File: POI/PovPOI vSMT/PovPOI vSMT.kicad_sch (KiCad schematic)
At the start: 22 parts, among them J2 Conn_01x08, J3 Conn_01x04, J4 Conn_01x08, J5 Conn_01x04, Q1 Q_NMOS_GDSD, SW1 SW_SPST, SW2 SW_SPST, U2 ADXL345BCCZ-RL7

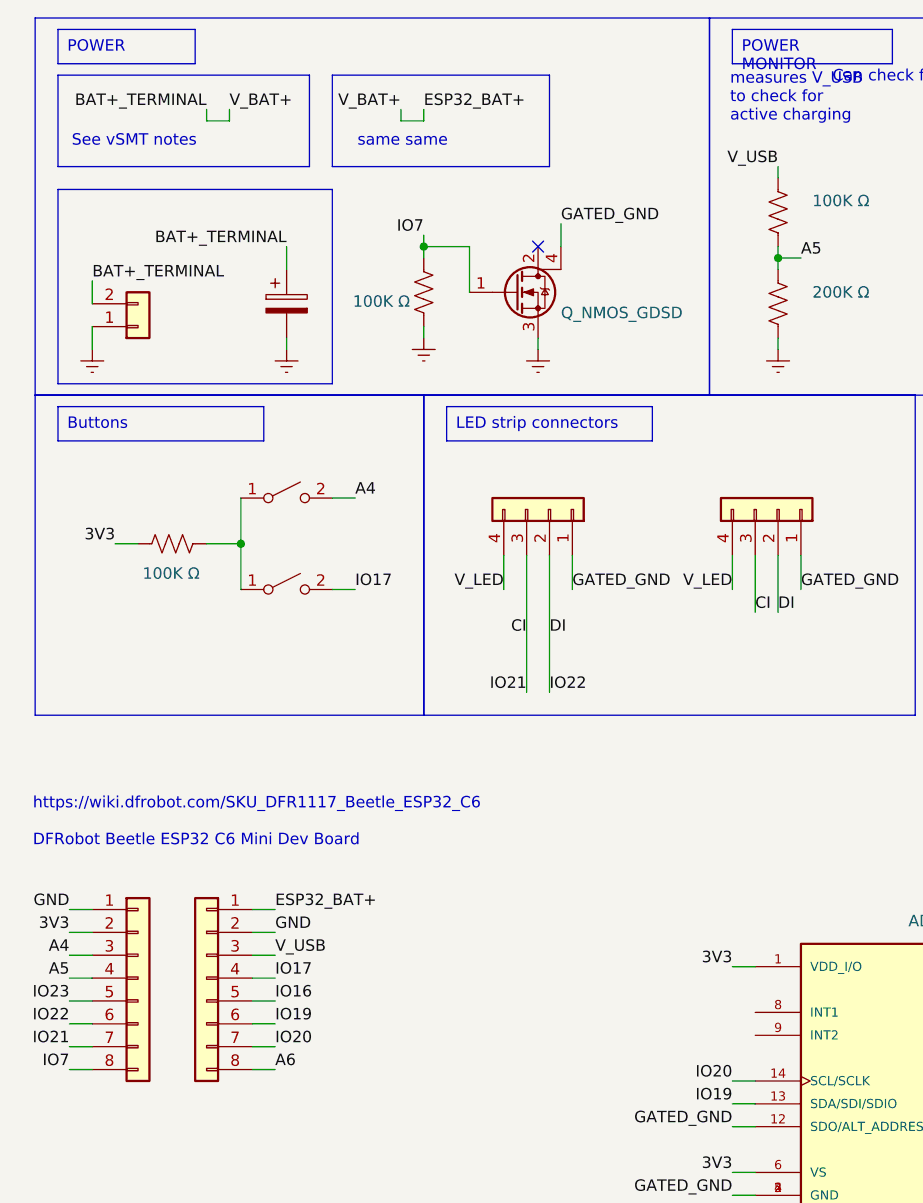
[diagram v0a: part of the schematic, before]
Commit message: Reloaded PovPOI vSMT from worklaptop
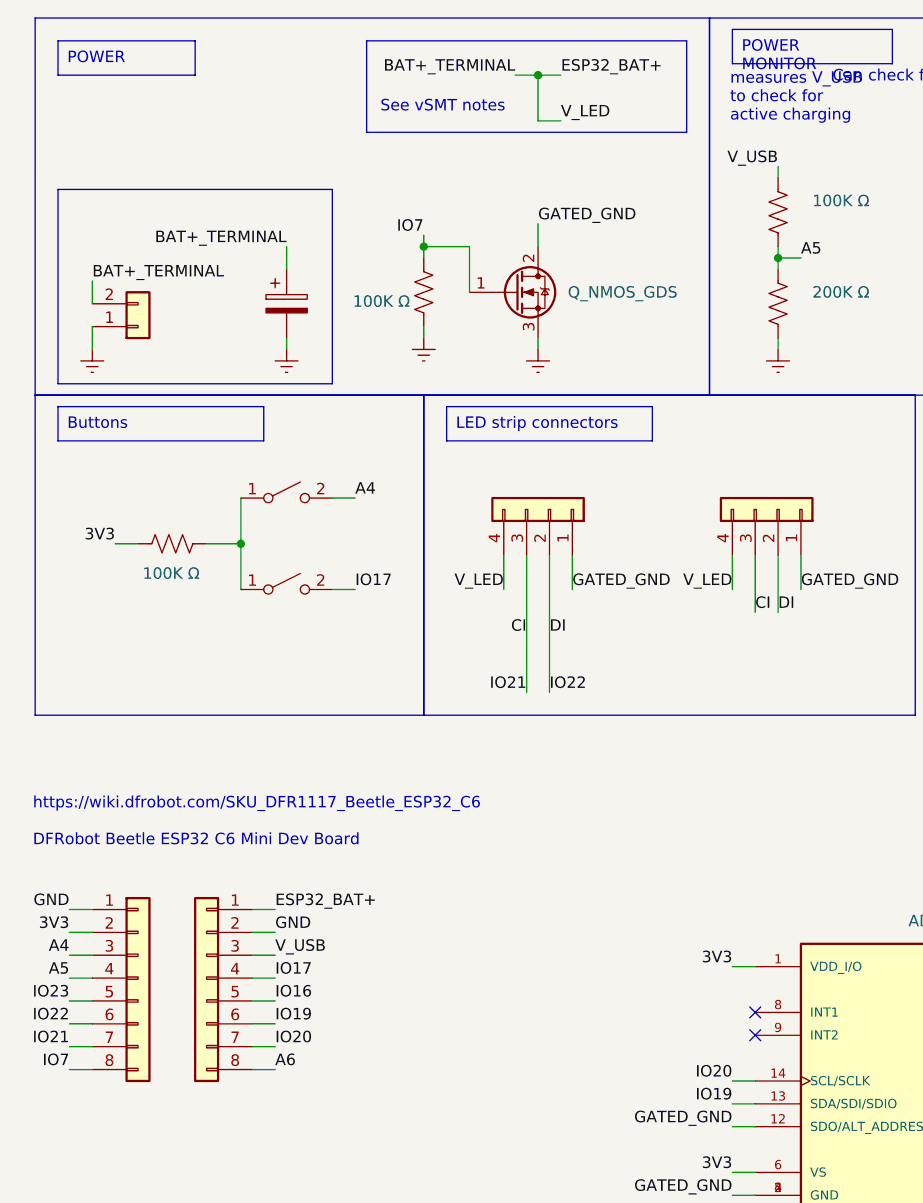
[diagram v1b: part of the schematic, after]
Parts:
- removed Q1: Q_NMOS_GDSD, Package_TO_SOT_SMD:TO-252-3_TabPin4, symbol Device:Q_NMOS_GDSD
- added Q2: Q_NMOS_GDS, Package_TO_SOT_SMD:TO-252-2, symbol Device:Q_NMOS_GDS
- C2: JLC (none) -> 0805
- R1, R5, R6: JLC (none) -> 0805; LCSC (none) -> C149504
- R3: JLC (none) -> 0805; LCSC (none) -> C17539
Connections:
- net V_LED is gone; now on net BAT+_TERMINAL: J3.4 (Pin_4), J5.4 (Pin_4)
- net GATED_GND: now also Q2.2 (D)
- net GND: now also Q2.3 (S)
- net IO7: now also Q2.1 (G)
- no-connect marks 3 -> 4
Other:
- note removed: "same same"
